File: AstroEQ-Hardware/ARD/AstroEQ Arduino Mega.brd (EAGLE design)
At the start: 101.6 x 53.3 mm, 18 parts, among them J1 POWER_JACKPTH, M0 Motor Driver, M1 Motor Driver

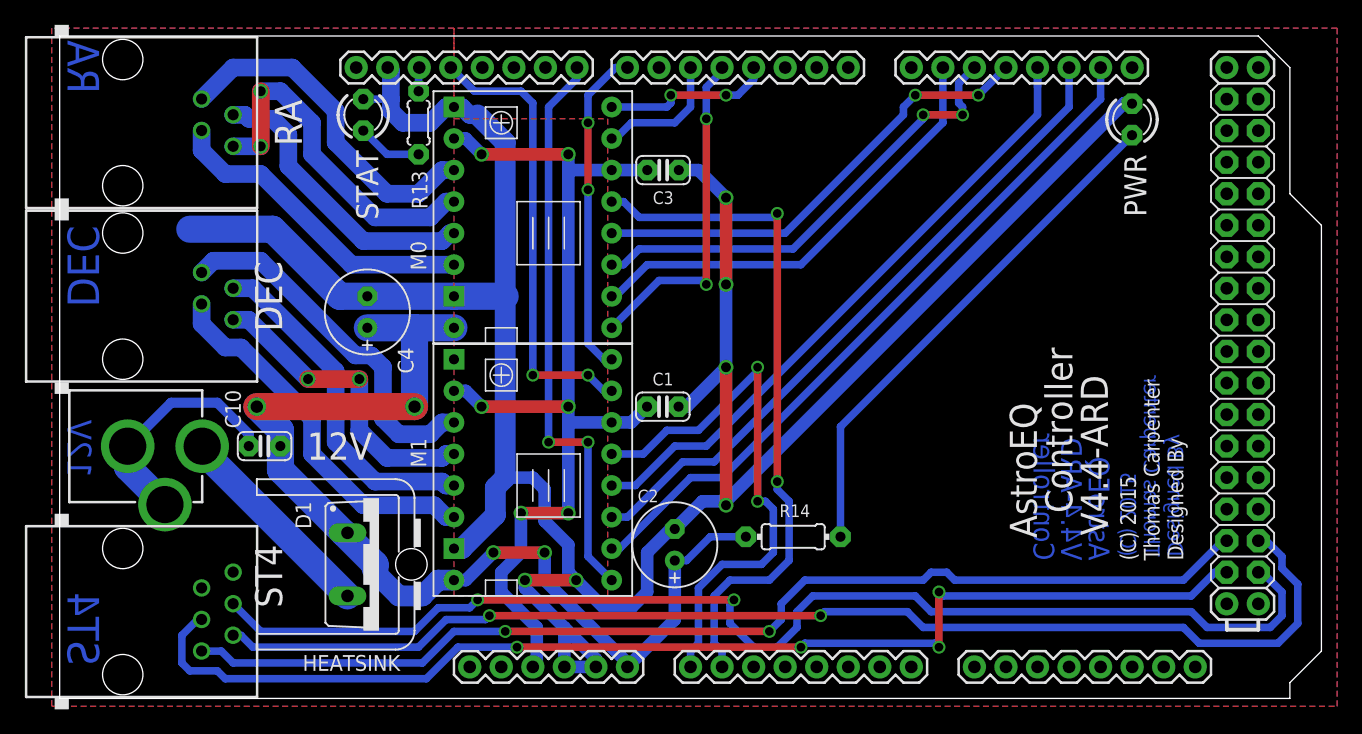
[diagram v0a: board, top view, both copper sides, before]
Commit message: Update PCB Logo
Add AstroEQ logo to PCB hardware designs.
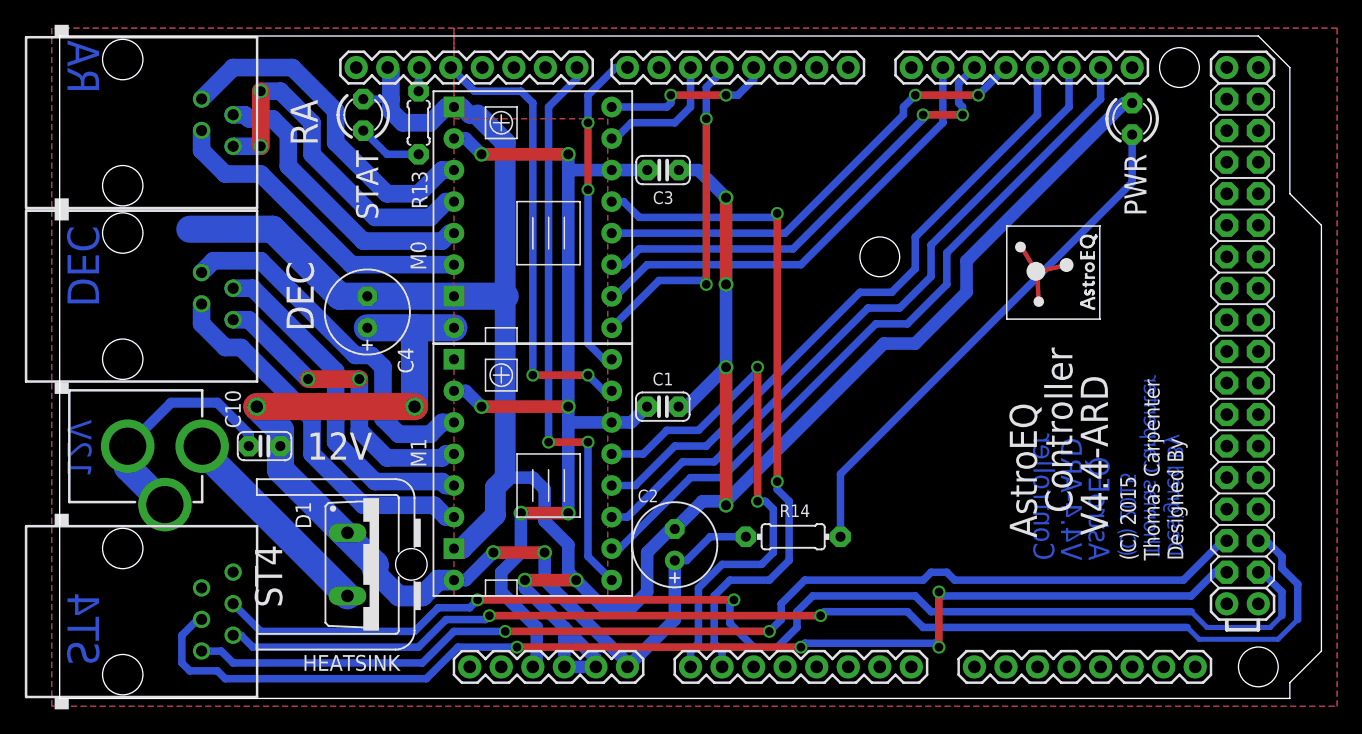
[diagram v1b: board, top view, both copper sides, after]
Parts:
- added LOGO1: ASTROEQ8MM, CompanyLogos:ASTROEQ
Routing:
- net GND: track 229.5 -> 230.9 mm
- net MS1-1: track 56.9 -> 58.4 mm
- net MS3-1: track 52.0 -> 53.5 mm
- net MS2-1: track 53.7 -> 55.2 mm
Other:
- board text added: "Make sure to show the ground plane. Type 'ratsnest' and press enter."
